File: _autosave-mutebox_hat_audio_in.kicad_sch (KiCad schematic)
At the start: 27 parts, among them J1 GPIO, U1 CAT24C256, U2 74LVC157, U3 PCM1862DBT, Y3 XO32

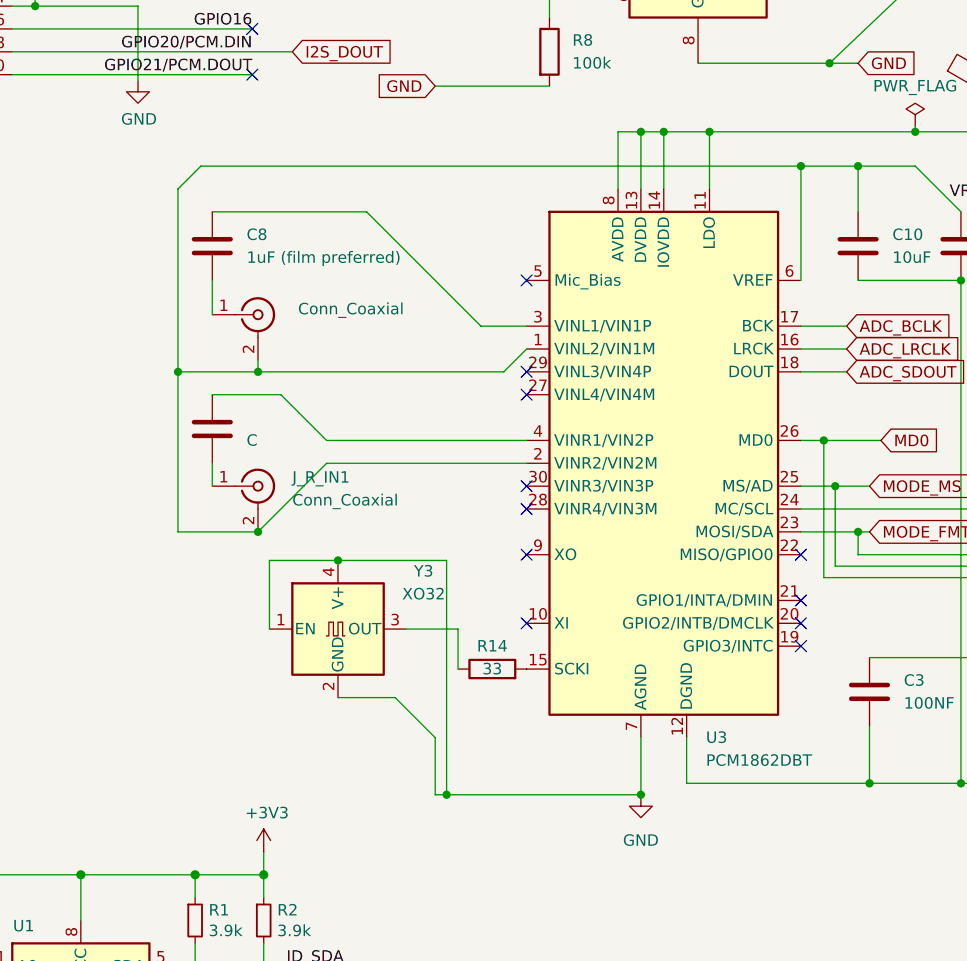
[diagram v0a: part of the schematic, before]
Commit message: Fixed RCA Jack symbols and footprints
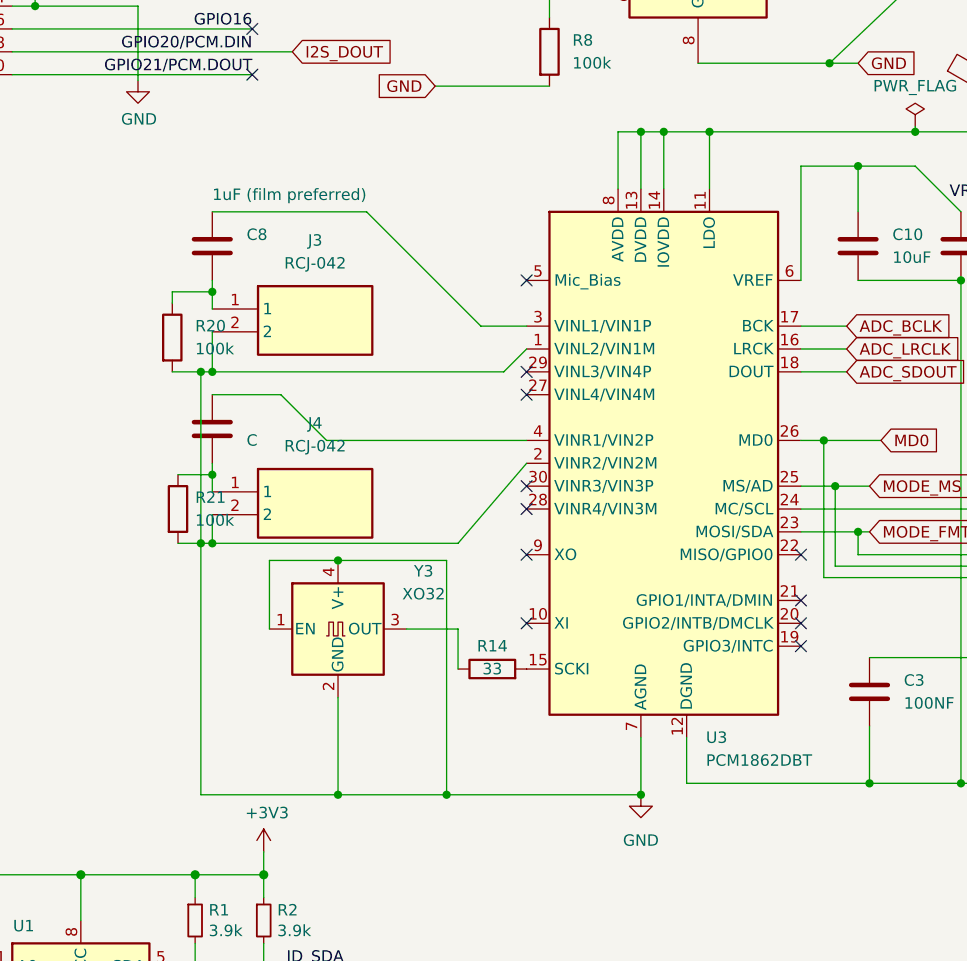
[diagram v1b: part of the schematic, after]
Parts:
- removed J_L_IN1, J_R_IN1: Conn_Coaxial, Connector_Audio:RCJ-043, symbol Connector:Conn_Coaxial
- added J3, J4: RCJ-042, RCJ-042:CUI_RCJ-042, symbol RCJ-042:RCJ-042
- added R20, R21: 100k, Resistor_SMD:R_0805_2012Metric_Pad1.20x1.40mm_HandSolder, symbol Device:R
- R11: footprint (none) -> Resistor_SMD:R_0805_2012Metric_Pad1.20x1.40mm_HandSolder
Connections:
- net GND: now also U3.1 (VINL2/VIN1M), U3.2 (VINR2/VIN2M), J3.2, J4.2, R20.2, R21.2
- net VREF: no longer U3.1 (VINL2/VIN1M), U3.2 (VINR2/VIN2M)
- net at C8.2: now also J3.1, R20.1
- net at C9.2: now also J4.1, R21.1
